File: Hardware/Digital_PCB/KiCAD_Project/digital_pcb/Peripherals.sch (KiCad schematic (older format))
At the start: 13 parts, among them U2 BNO055, Y2 32.768kHz

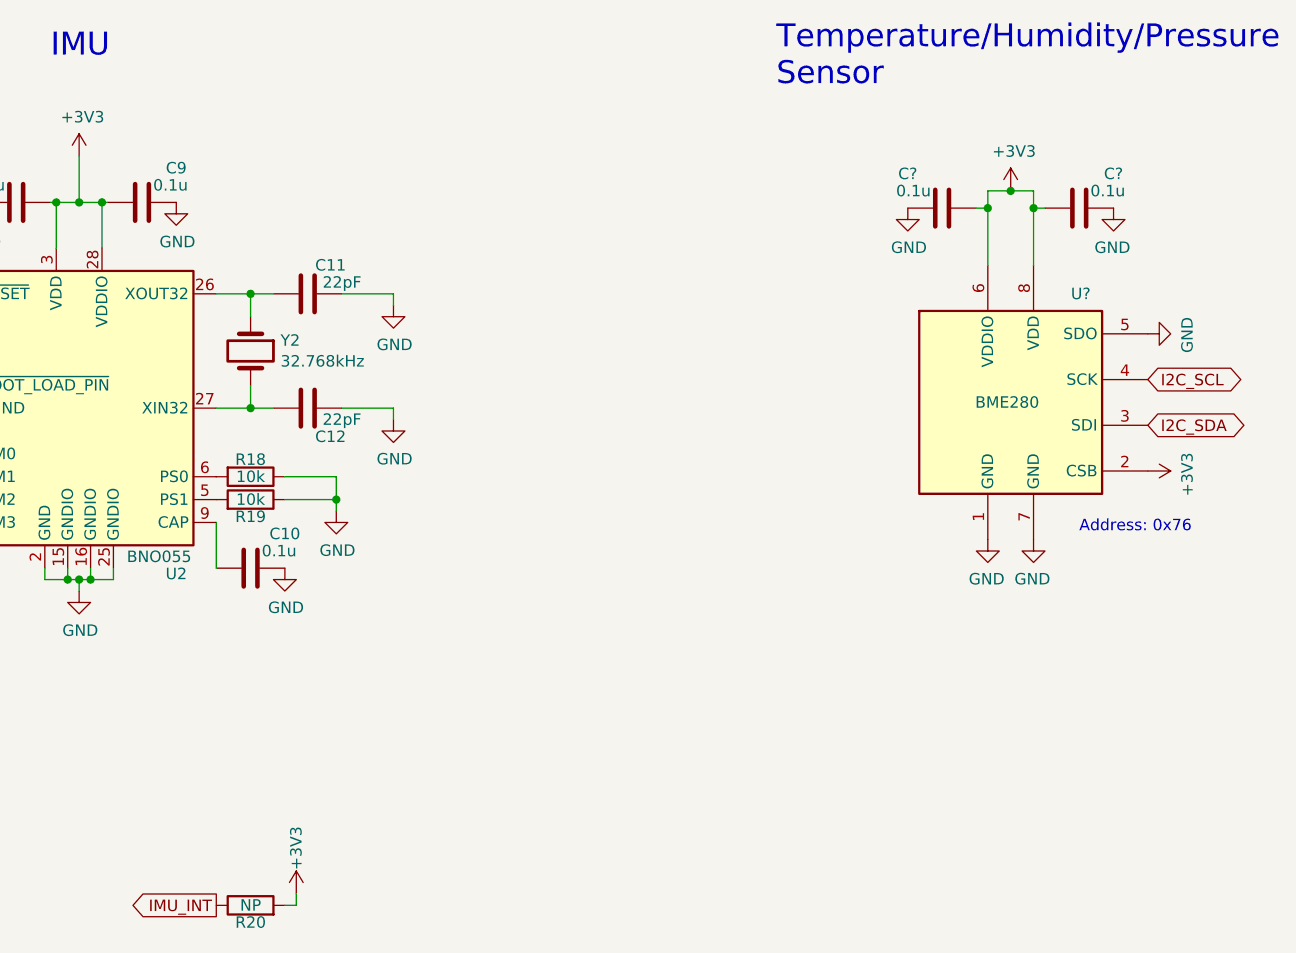
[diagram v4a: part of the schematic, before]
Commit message: Update footprints
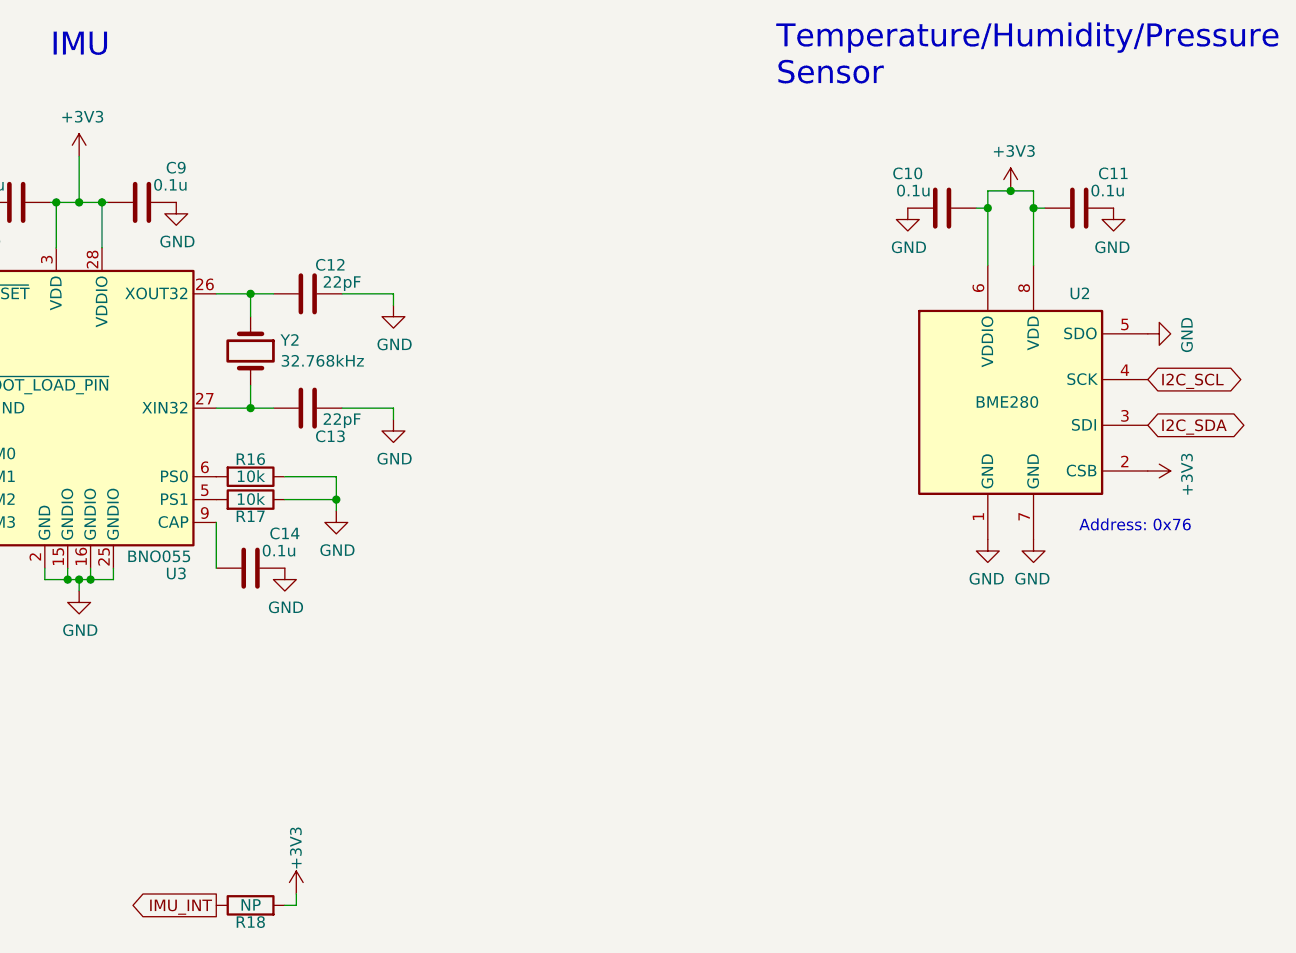
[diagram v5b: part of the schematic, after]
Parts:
- C10, C11: renamed from C?; footprint Capacitors_SMD:C_0603_HandSoldering -> Capacitor_SMD:C_0603_1608Metric
- C12: renamed from C11; footprint Capacitors_SMD:C_0603_HandSoldering -> Capacitor_SMD:C_0603_1608Metric
- C13: renamed from C12; footprint Capacitors_SMD:C_0603_HandSoldering -> Capacitor_SMD:C_0603_1608Metric
- C14: renamed from C10; footprint Capacitors_SMD:C_0603_HandSoldering -> Capacitor_SMD:C_0603_1608Metric
- C8, C9: footprint Capacitors_SMD:C_0603_HandSoldering -> Capacitor_SMD:C_0603_1608Metric
- R16: renamed from R18; footprint Resistors_SMD:R_0603_HandSoldering -> Resistor_SMD:R_0603_1608Metric
- R17: renamed from R19; footprint Resistors_SMD:R_0603_HandSoldering -> Resistor_SMD:R_0603_1608Metric
- R18: renamed from R20; footprint Resistors_SMD:R_0603_HandSoldering -> Resistor_SMD:R_0603_1608Metric
- gave numbers to parts that had none: 1
- renumbered U2 to U3
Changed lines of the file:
@@
 F 0 "C8" V 3325 2550 50  0000 C CNN
 F 1 "0.1u" V 3400 2575 50  0000 C CNN
-F 2 "Capacitors_SMD:C_0603_HandSoldering" H 3513 2550 50  0001 C CNN
+F 2 "Capacitor_SMD:C_0603_1608Metric" H 3513 2550 50  0001 C CNN
 F 3 "~" H 3475 2700 50  0001 C CNN
 F 4 "1-0000007" H 3475 2700 50  0001 C CNN "Internal Part Number"
@@
 F 0 "C9" V 3875 2550 50  0000 C CNN
 F 1 "0.1u" V 3950 2575 50  0000 C CNN
-F 2 "Capacitors_SMD:C_0603_HandSoldering" H 4063 2550 50  0001 C CNN
+F 2 "Capacitor_SMD:C_0603_1608Metric" H 4063 2550 50  0001 C CNN
 F 3 "~" H 4025 2700 50  0001 C CNN
 F 4 "1-0000007" H 4025 2700 50  0001 C CNN "Internal Part Number"
@@
 	3650 2700 3625 2700
 $Comp
-L power:GND #PWR031
+L power:GND #PWR040
 U 1 1 5DFD929D
 P 3750 4400
-F 0 "#PWR031" H 3750 4150 50  0001 C CNN
+F 0 "#PWR040" H 3750 4150 50  0001 C CNN
 F 1 "GND" H 3755 4227 50  0000 C CNN
 F 2 "" H 3750 4400 50  0001 C CNN
@@
 $EndComp
 $Comp
-L power:GND #PWR027
+L power:GND #PWR025
 U 1 1 5DFD9B68
 P 3325 2700
-F 0 "#PWR027" H 3325 2450 50  0001 C CNN
+F 0 "#PWR025" H 3325 2450 50  0001 C CNN
 F 1 "GND" H 3330 2527 50  0000 C CNN
 F 2 "" H 3325 2700 50  0001 C CNN
@@
 $EndComp
 $Comp
-L power:GND #PWR032
+L power:GND #PWR026
 U 1 1 5DFD9FE1
 P 4175 2700
-F 0 "#PWR032" H 4175 2450 50  0001 C CNN
+F 0 "#PWR026" H 4175 2450 50  0001 C CNN
 F 1 "GND" H 4180 2527 50  0000 C CNN
 F 2 "" H 4175 2700 50  0001 C CNN
@@
 $EndComp
 $Comp
-L power:+3V3 #PWR030
+L power:+3V3 #PWR023
 U 1 1 5DFDA366
 P 3750 2500
-F 0 "#PWR030" H 3750 2350 50  0001 C CNN
+F 0 "#PWR023" H 3750 2350 50  0001 C CNN
 F 1 "+3V3" H 3765 2673 50  0000 C CNN
 F 2 "" H 3750 2500 50  0001 C CNN
@@
 P 4500 4300
 AR Path="/5DFDAE92" Ref="C?"  Part="1"
-AR Path="/5DFD7345/5DFDAE92" Ref="C10"  Part="1"
-F 0 "C10" V 4350 4150 50  0000 C CNN
+AR Path="/5DFD7345/5DFDAE92" Ref="C14"  Part="1"
+F 0 "C14" V 4350 4150 50  0000 C CNN
 F 1 "0.1u" V 4425 4175 50  0000 C CNN
-F 2 "Capacitors_SMD:C_0603_HandSoldering" H 4538 4150 50  0001 C CNN
+F 2 "Capacitor_SMD:C_0603_1608Metric" H 4538 4150 50  0001 C CNN
 F 3 "~" H 4500 4300 50  0001 C CNN
 F 4 "1-0000007" H 4500 4300 50  0001 C CNN "Internal Part Number"
@@
 $EndComp
 $Comp
-L power:GND #PWR033
+L power:GND #PWR039
 U 1 1 5DFDB36A
 P 4650 4300
-F 0 "#PWR033" H 4650 4050 50  0001 C CNN
+F 0 "#PWR039" H 4650 4050 50  0001 C CNN
 F 1 "GND" H 4655 4127 50  0000 C CNN
 F 2 "" H 4650 4300 50  0001 C CNN
@@
 $EndComp
 $Comp
-L Device:R R18
+L Device:R R16
 U 1 1 5DFDB705
 P 4500 3900
-F 0 "R18" V 4425 3900 50  0000 C CNN
+F 0 "R16" V 4425 3900 50  0000 C CNN
 F 1 "10k" V 4500 3900 50  0000 C CNN
-F 2 "Resistors_SMD:R_0603_HandSoldering" V 4430 3900 50  0001 C CNN
+F 2 "Resistor_SMD:R_0603_1608Metric" V 4430 3900 50  0001 C CNN
 F 3 "~" H 4500 3900 50  0001 C CNN
 F 4 "1-0000010" H 4500 3900 50  0001 C CNN "Internal Part Number"
@@
 	4350 4300 4350 4100
 $Comp
-L Device:R R19
+L Device:R R17
 U 1 1 5DFDD648
 P 4500 4000
-F 0 "R19" V 4425 4000 50  0000 C CNN
+F 0 "R17" V 4425 4000 50  0000 C CNN
 F 1 "10k" V 4500 4000 50  0000 C CNN
-F 2 "Resistors_SMD:R_0603_HandSoldering" V 4430 4000 50  0001 C CNN
+F 2 "Resistor_SMD:R_0603_1608Metric" V 4430 4000 50  0001 C CNN
 F 3 "~" H 4500 4000 50  0001 C CNN
 F 4 "1-0000010" H 4500 4000 50  0001 C CNN "Internal Part Number"
@@
 $EndComp
 $Comp
-L power:GND #PWR035
+L power:GND #PWR036
 U 1 1 5DFDDB88
 P 4875 4050
-F 0 "#PWR035" H 4875 3800 50  0001 C CNN
+F 0 "#PWR036" H 4875 3800 50  0001 C CNN
 F 1 "GND" H 4880 3877 50  0000 C CNN
 F 2 "" H 4875 4050 50  0001 C CNN
@@
 	4500 3600 4350 3600
 $Comp
-L Device:C C11
+L Device:C C12
 U 1 1 5DFDF71F
 P 4750 3100
-F 0 "C11" V 4625 3200 50  0000 C CNN
+F 0 "C12" V 4625 3200 50  0000 C CNN
 F 1 "22pF" V 4700 3250 50  0000 C CNN
-F 2 "Capacitors_SMD:C_0603_HandSoldering" H 4788 2950 50  0001 C CNN
+F 2 "Capacitor_SMD:C_0603_1608Metric" H 4788 2950 50  0001 C CNN
 F 3 "~" H 4750 3100 50  0001 C CNN
 F 4 "1-0000020" H 4750 3100 50  0001 C CNN "Internal Part Number"
@@
 $EndComp
 $Comp
-L Device:C C12
+L Device:C C13
 U 1 1 5DFDFF1D
 P 4750 3600
-F 0 "C12" V 4875 3700 50  0000 C CNN
+F 0 "C13" V 4875 3700 50  0000 C CNN
 F 1 "22pF" V 4800 3750 50  0000 C CNN
-F 2 "Capacitors_SMD:C_0603_HandSoldering" H 4788 3450 50  0001 C CNN
+F 2 "Capacitor_SMD:C_0603_1608Metric" H 4788 3450 50  0001 C CNN
 F 3 "~" H 4750 3600 50  0001 C CNN
 F 4 "1-0000020" H 4750 3600 50  0001 C CNN "Internal Part Number"
@@
 	5125 3600 5125 3650
 $Comp
-L power:GND #PWR037
+L power:GND #PWR033
 U 1 1 5DFE16EA
 P 5125 3650
-F 0 "#PWR037" H 5125 3400 50  0001 C CNN
+F 0 "#PWR033" H 5125 3400 50  0001 C CNN
 F 1 "GND" H 5130 3477 50  0000 C CNN
 F 2 "" H 5125 3650 50  0001 C CNN
@@
 $EndComp
 $Comp
-L power:GND #PWR036
+L power:GND #PWR029
 U 1 1 5DFE1907
 P 5125 3150
-F 0 "#PWR036" H 5125 2900 50  0001 C CNN
+F 0 "#PWR029" H 5125 2900 50  0001 C CNN
 F 1 "GND" H 5130 2977 50  0000 C CNN
 F 2 "" H 5125 3150 50  0001 C CNN
@@
 $EndComp
 $Comp
-L lib_sch:BNO055 U2
+L lib_sch:BNO055 U3
 U 1 1 5DFE2566
 P 3750 3600
-F 0 "U2" H 4175 2875 50  0000 C CNN
+F 0 "U3" H 4175 2875 50  0000 C CNN
 F 1 "BNO055" H 4100 2950 50  0000 C CNN
 F 2 "lib_fp:LGA28R50P4X10_380X520X100" H 4000 2950 50  0001 L CNN
@@
 	3700 4350 3750 4350
 $Comp
-L power:GND #PWR025
+L power:GND #PWR032
 U 1 1 5DFE4AE9
 P 3000 3600
-F 0 "#PWR025" H 3000 3350 50  0001 C CNN
+F 0 "#PWR032" H 3000 3350 50  0001 C CNN
 F 1 "GND" V 3005 3472 50  0000 R CNN
 F 2 "" H 3000 3600 50  0001 C CNN
@@
 	3000 3600 3150 3600
 $Comp
-L power:+3V3 #PWR024
+L power:+3V3 #PWR031
 U 1 1 5DFE56B9
 P 3000 3500
-F 0 "#PWR024" H 3000 3350 50  0001 C CNN
+F 0 "#PWR031" H 3000 3350 50  0001 C CNN
 F 1 "+3V3" V 3015 3628 50  0000 L CNN
 F 2 "" H 3000 3500 50  0001 C CNN
@@
 	3000 3500 3150 3500
 $Comp
-L power:GND #PWR026
+L power:GND #PWR035
 U 1 1 5DFE66D6
 P 3000 4000
-F 0 "#PWR026" H 3000 3750 50  0001 C CNN
+F 0 "#PWR035" H 3000 3750 50  0001 C CNN
 F 1 "GND" V 3005 3872 50  0000 R CNN
 F 2 "" H 3000 4000 50  0001 C CNN
@@
 	4650 5775 4700 5775
 $Comp
-L power:+3V3 #PWR034
+L power:+3V3 #PWR041
 U 1 1 5DFE9D21
 P 4700 5725
-F 0 "#PWR034" H 4700 5575 50  0001 C CNN
+F 0 "#PWR041" H 4700 5575 50  0001 C CNN
 F 1 "+3V3" V 4700 5925 50  0000 C CNN
 F 2 "" H 4700 5725 50  0001 C CNN
@@
 $EndComp
 $Comp
-L Device:R R20
+L Device:R R18
 U 1 1 5DFE9D1B
 P 4500 5775
-F 0 "R20" V 4425 5775 50  0000 C CNN
+F 0 "R18" V 4425 5775 50  0000 C CNN
 F 1 "NP" V 4500 5775 50  0000 C CNN
-F 2 "Resistors_SMD:R_0603_HandSoldering" V 4430 5775 50  0001 C CNN
+F 2 "Resistor_SMD:R_0603_1608Metric" V 4430 5775 50  0001 C CNN
 F 3 "~" H 4500 5775 50  0001 C CNN
 F 4 "1-0000010" H 4500 5775 50  0001 C CNN "Internal Part Number"
@@
 IMU_INT
 $Comp
-L Sensor:BME280 U?
+L Sensor:BME280 U2
 U 1 1 5FDBCAD6
 P 7825 3575
-F 0 "U?" H 8175 4050 50  0000 R CNN
+F 0 "U2" H 8175 4050 50  0000 R CNN
 F 1 "BME280" H 7950 3575 50  0000 R CNN
 F 2 "Package_LGA:Bosch_LGA-8_2.5x2.5mm_P0.65mm_ClockwisePinNumbering" H 9325 3125 50  0001 C CNN
@@
 P 7525 2725
 AR Path="/5FDBD897" Ref="C?"  Part="1"
-AR Path="/5DFD7345/5FDBD897" Ref="C?"  Part="1"
-F 0 "C?" V 7375 2575 50  0000 C CNN
+AR Path="/5DFD7345/5FDBD897" Ref="C10"  Part="1"
+F 0 "C10" V 7375 2575 50  0000 C CNN
 F 1 "0.1u" V 7450 2600 50  0000 C CNN
-F 2 "Capacitors_SMD:C_0603_HandSoldering" H 7563 2575 50  0001 C CNN
+F 2 "Capacitor_SMD:C_0603_1608Metric" H 7563 2575 50  0001 C CNN
 F 3 "~" H 7525 2725 50  0001 C CNN
 F 4 "1-0000007" H 7525 2725 50  0001 C CNN "Internal Part Number"
@@
 $EndComp
 $Comp
-L power:GND #PWR?
+L power:GND #PWR027
 U 1 1 5FDBD89D
 P 7375 2725
-F 0 "#PWR?" H 7375 2475 50  0001 C CNN
+F 0 "#PWR027" H 7375 2475 50  0001 C CNN
 F 1 "GND" H 7380 2552 50  0000 C CNN
 F 2 "" H 7375 2725 50  0001 C CNN
@@
 $EndComp
 $Comp
-L power:+3V3 #PWR?
+L power:+3V3 #PWR024
 U 1 1 5FDBD8A3
 P 7825 2650
-F 0 "#PWR?" H 7825 2500 50  0001 C CNN
+F 0 "#PWR024" H 7825 2500 50  0001 C CNN
 F 1 "+3V3" H 7840 2823 50  0000 C CNN
 F 2 "" H 7825 2650 50  0001 C CNN
@@
 P 8125 2725
 AR Path="/5FDC0A1A" Ref="C?"  Part="1"
-AR Path="/5DFD7345/5FDC0A1A" Ref="C?"  Part="1"
-F 0 "C?" V 7975 2575 50  0000 C CNN
+AR Path="/5DFD7345/5FDC0A1A" Ref="C11"  Part="1"
+F 0 "C11" V 7975 2575 50  0000 C CNN
 F 1 "0.1u" V 8050 2600 50  0000 C CNN
-F 2 "Capacitors_SMD:C_0603_HandSoldering" H 8163 2575 50  0001 C CNN
+F 2 "Capacitor_SMD:C_0603_1608Metric" H 8163 2575 50  0001 C CNN
 F 3 "~" H 8125 2725 50  0001 C CNN
 F 4 "1-0000007" H 8125 2725 50  0001 C CNN "Internal Part Number"
@@
 $EndComp
 $Comp
-L power:GND #PWR?
+L power:GND #PWR028
 U 1 1 5FDC0A20
 P 8275 2725
-F 0 "#PWR?" H 8275 2475 50  0001 C CNN
+F 0 "#PWR028" H 8275 2475 50  0001 C CNN
 F 1 "GND" H 8280 2552 50  0000 C CNN
 F 2 "" H 8275 2725 50  0001 C CNN
@@
 	7725 2725 7725 2975
 $Comp
-L power:+3V3 #PWR?
+L power:+3V3 #PWR034
 U 1 1 5FDC656D
 P 8425 3875
-F 0 "#PWR?" H 8425 3725 50  0001 C CNN
+F 0 "#PWR034" H 8425 3725 50  0001 C CNN
 F 1 "+3V3" H 8440 4048 50  0000 C CNN
 F 2 "" H 8425 3875 50  0001 C CNN
@@
 $EndComp
 $Comp
-L power:GND #PWR?
+L power:GND #PWR030
 U 1 1 5FDC75ED
 P 8425 3275
-F 0 "#PWR?" H 8425 3025 50  0001 C CNN
+F 0 "#PWR030" H 8425 3025 50  0001 C CNN
 F 1 "GND" H 8430 3102 50  0000 C CNN
 F 2 "" H 8425 3275 50  0001 C CNN
@@
 I2C_SDA
 $Comp
-L power:GND #PWR?
+L power:GND #PWR037
 U 1 1 5FDC7CCA
 P 7725 4175
-F 0 "#PWR?" H 7725 3925 50  0001 C CNN
+F 0 "#PWR037" H 7725 3925 50  0001 C CNN
 F 1 "GND" H 7730 4002 50  0000 C CNN
 F 2 "" H 7725 4175 50  0001 C CNN
@@
 $EndComp
 $Comp
-L power:GND #PWR?
+L power:GND #PWR038
 U 1 1 5FDC8367
 P 7925 4175
-F 0 "#PWR?" H 7925 3925 50  0001 C CNN
+F 0 "#PWR038" H 7925 3925 50  0001 C CNN
 F 1 "GND" H 7930 4002 50  0000 C CNN
 F 2 "" H 7925 4175 50  0001 C CNN
